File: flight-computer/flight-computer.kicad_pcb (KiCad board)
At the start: 4 copper layers, 83.7 x 62.9 mm, 96 parts, among them J1 MicroSD Slot, J2 USB_C_Receptacle_USB2.0_16P, J3 SMA_Coax, J4 Conn_01x02, J5 ARM, Q1 PMOS, Q2 NMOS, SW1 SW_Push, SW2 SW_Push, U1 RP2040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

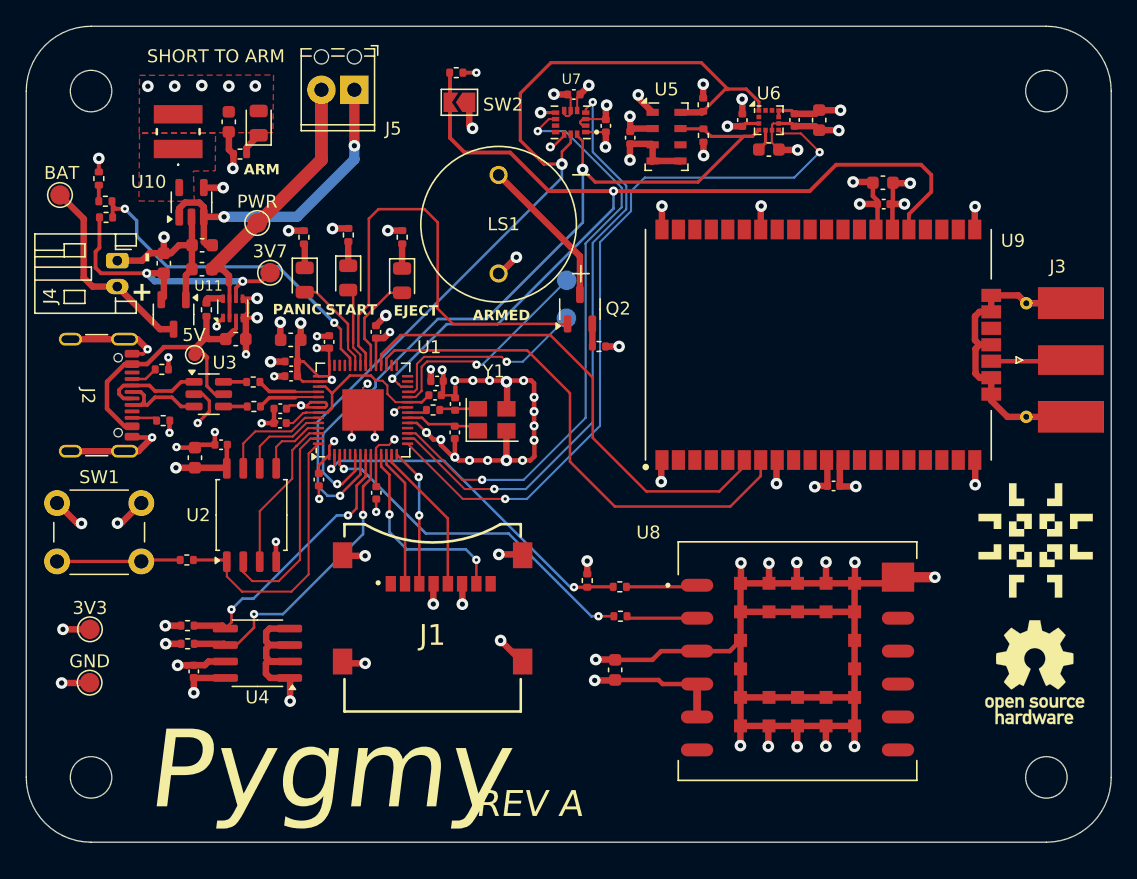
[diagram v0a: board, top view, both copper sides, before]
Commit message: Update silkscreen to show reset pins.
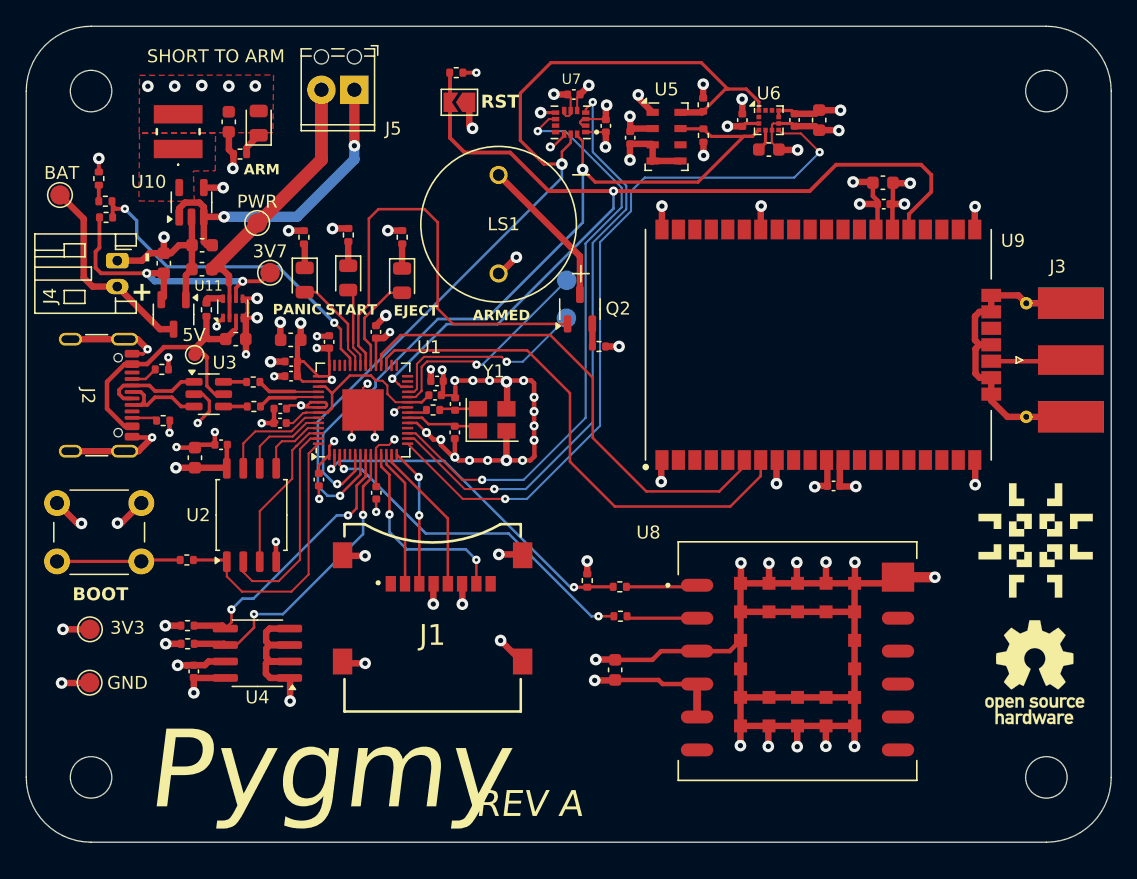
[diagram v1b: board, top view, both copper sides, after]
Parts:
- renumbered SW2 to RST
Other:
- board text added: "BOOT"
- board text added: "RST"
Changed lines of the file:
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@@
 		(tags "test point SMD pad")
 		(property "Reference" "3V3"
-			(at 0 -1.648 0)
+			(at 2.8968 -0.1194 0)
 			(layer "F.SilkS")
 			(effects
@@
 		(descr "SMD Solder Jumper, 1x1.5mm Triangular Pads, 0.3mm gap, open")
 		(tags "solder jumper open")
-		(property "Reference" "SW2"
+		(property "Reference" "RST"
 			(at -3.3666 -0.1778 180)
 			(layer "F.SilkS")
+			(hide yes)
 			(effects
 				(font
@@
 		(tags "test point SMD pad")
 		(property "Reference" "GND"
-			(at 0 -1.648 0)
+			(at 2.9222 0.0158 0)
 			(layer "F.SilkS")
 			(effects
@@
 			(at 3.25 -2 0)
 			(layer "F.SilkS")
+			(hide yes)
 			(effects
 				(font
@@
 		)
 	)
+	(gr_text "RST"
+		(at 119.25 77 0)
+		(layer "F.SilkS")
+		(effects
+			(font
+				(size 1 1)
+				(thickness 0.2)
+				(bold yes)
+			)
+			(justify left bottom)
+		)
+	)
+	(gr_text "BOOT"
+		(at 87.75 115 0)
+		(layer "F.SilkS")
+		(effects
+			(font
+				(size 1 1)
+				(thickness 0.2)
+				(bold yes)
+			)
+			(justify left bottom)
+		)
+	)
